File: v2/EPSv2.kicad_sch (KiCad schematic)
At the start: 38 parts, among them J1 Conn_01x02, J2 Conn_01x03, J3 Conn_01x03, J4 5037630491, J5 2P 21700 Cell Holder, J6 5037630491, J7 1053091102, J8 1053091102, J9 1053091102

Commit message: preliminary layout
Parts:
- renumbered J2 to J1, J3 to J2, J1 to J3
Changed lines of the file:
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@@
 		(on_board yes)
 		(dnp no)
-		(property "Reference" "J1"
+		(property "Reference" "J3"
 			(at 65.024 44.958 0)
 			(effects
@@
 			(project ""
 				(path "/61d36b12-c329-4dd2-b08b-b63678fc7b25"
-					(reference "J1")
+					(reference "J3")
 					(unit 1)
 				)
@@
 		(dnp no)
 		(fields_autoplaced yes)
-		(property "Reference" "#PWR08"
+		(property "Reference" "#PWR07"
 			(at 80.01 52.07 0)
 			(effects
@@
 			(project "EPSv2"
 				(path "/61d36b12-c329-4dd2-b08b-b63678fc7b25"
-					(reference "#PWR08")
+					(reference "#PWR07")
 					(unit 1)
 				)
@@
 		(dnp no)
 		(fields_autoplaced yes)
-		(property "Reference" "J2"
+		(property "Reference" "J1"
 			(at 41.91 191.77 0)
 			(effects
@@
 			(project ""
 				(path "/61d36b12-c329-4dd2-b08b-b63678fc7b25"
-					(reference "J2")
+					(reference "J1")
 					(unit 1)
 				)
@@
 		(dnp no)
 		(fields_autoplaced yes)
-		(property "Reference" "J3"
+		(property "Reference" "J2"
 			(at 41.91 212.09 0)
 			(effects
@@
 			(project "EPSv2"
 				(path "/61d36b12-c329-4dd2-b08b-b63678fc7b25"
-					(reference "J3")
+					(reference "J2")
 					(unit 1)
 				)
@@
 		(dnp no)
 		(fields_autoplaced yes)
-		(property "Reference" "#PWR07"
+		(property "Reference" "#PWR08"
 			(at 106.68 55.88 0)
 			(effects
@@
 			(project "EPSv1"
 				(path "/61d36b12-c329-4dd2-b08b-b63678fc7b25"
-					(reference "#PWR07")
+					(reference "#PWR08")
 					(unit 1)
 				)

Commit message: battery charging routing
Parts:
- removed C1, C10, C2, C3, C4, C5, C6, C7, C8, C9: 10uF 0603, Rocketry_Easyeda:C0603, symbol Rocketry_Easyeda:CL10A106KP8NNNC (10uF 0603)
- added C1, C2: 47uF, Capacitor_SMD:C_0603_1608Metric, symbol Device:C
- J4, J6: footprint CON_5037630491 -> Rocketry_Manual:CON_5037630491
- J7, J8, J9: footprint CON_1053091102 -> Rocketry_Manual:CON_1053091102
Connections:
- net +3.3V: now also C1.1
- net GND: now also C1.2, C2.2
- net STM32L432KCUx/+3V3A: now also C2.1
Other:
- moved on the sheet: L1

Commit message: routing done
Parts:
- removed R5, R6, R7: 100k 0603, Rocketry_Easyeda:R0603, symbol Rocketry_Easyeda:0603WAF1003T5E (100k 0603)
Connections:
- net INA199_1/IN- renamed LM7310_9V/VOUT
- net INA199_2/IN- renamed LM7310_5V/VOUT
- net INA199_3/IN- renamed LM7310_3.3V/VOUT
- net PB0 renamed TEMP_1
- net PB1 renamed TEMP_2
- no-connect marks 0 -> 4
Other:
- removed sheet INA199_1
- removed sheet INA199_2
- removed sheet INA199_3
- removed sheet LM66200_4
- removed sheet LM66200_5
- removed sheet LM66200_6
- added sheet LM7310_3.3V (blocks/LM73100.kicad_sch)
- added sheet LM7310_5V (blocks/LM73100.kicad_sch)
- added sheet LM7310_9V (blocks/LM73100.kicad_sch)
- sheet STM32L432KCUx ports: added PB3, PB4, PB5, PB6, PB7; removed none
- note removed: "100k pulldowns to keep the default state ON"
- moved on the sheet: J7, J8, J9

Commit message: CAN txrx
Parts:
- J7, J8, J9: footprint Rocketry_Manual:CON_1053091102 -> Rocketry_Manual:1054301102; symbol Rocketry_Manual:1053091102 -> Rocketry_Manual:1054301102
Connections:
- net GND: now also J4.2 (GND), J6.2 (GND)
- net CAN_TX: now reaches J6.3 (CANH)
- net CAN_TX: now also J4.3 (CANH)
- net CAN_RX: now reaches J6.4 (CANL)
- net CAN_RX: now also J4.4 (CANL)
- no-connect marks 4 -> 2
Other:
- sheet STM32L432KCUx ports: added PA11, PA12; removed PA8
- moved on the sheet: J4

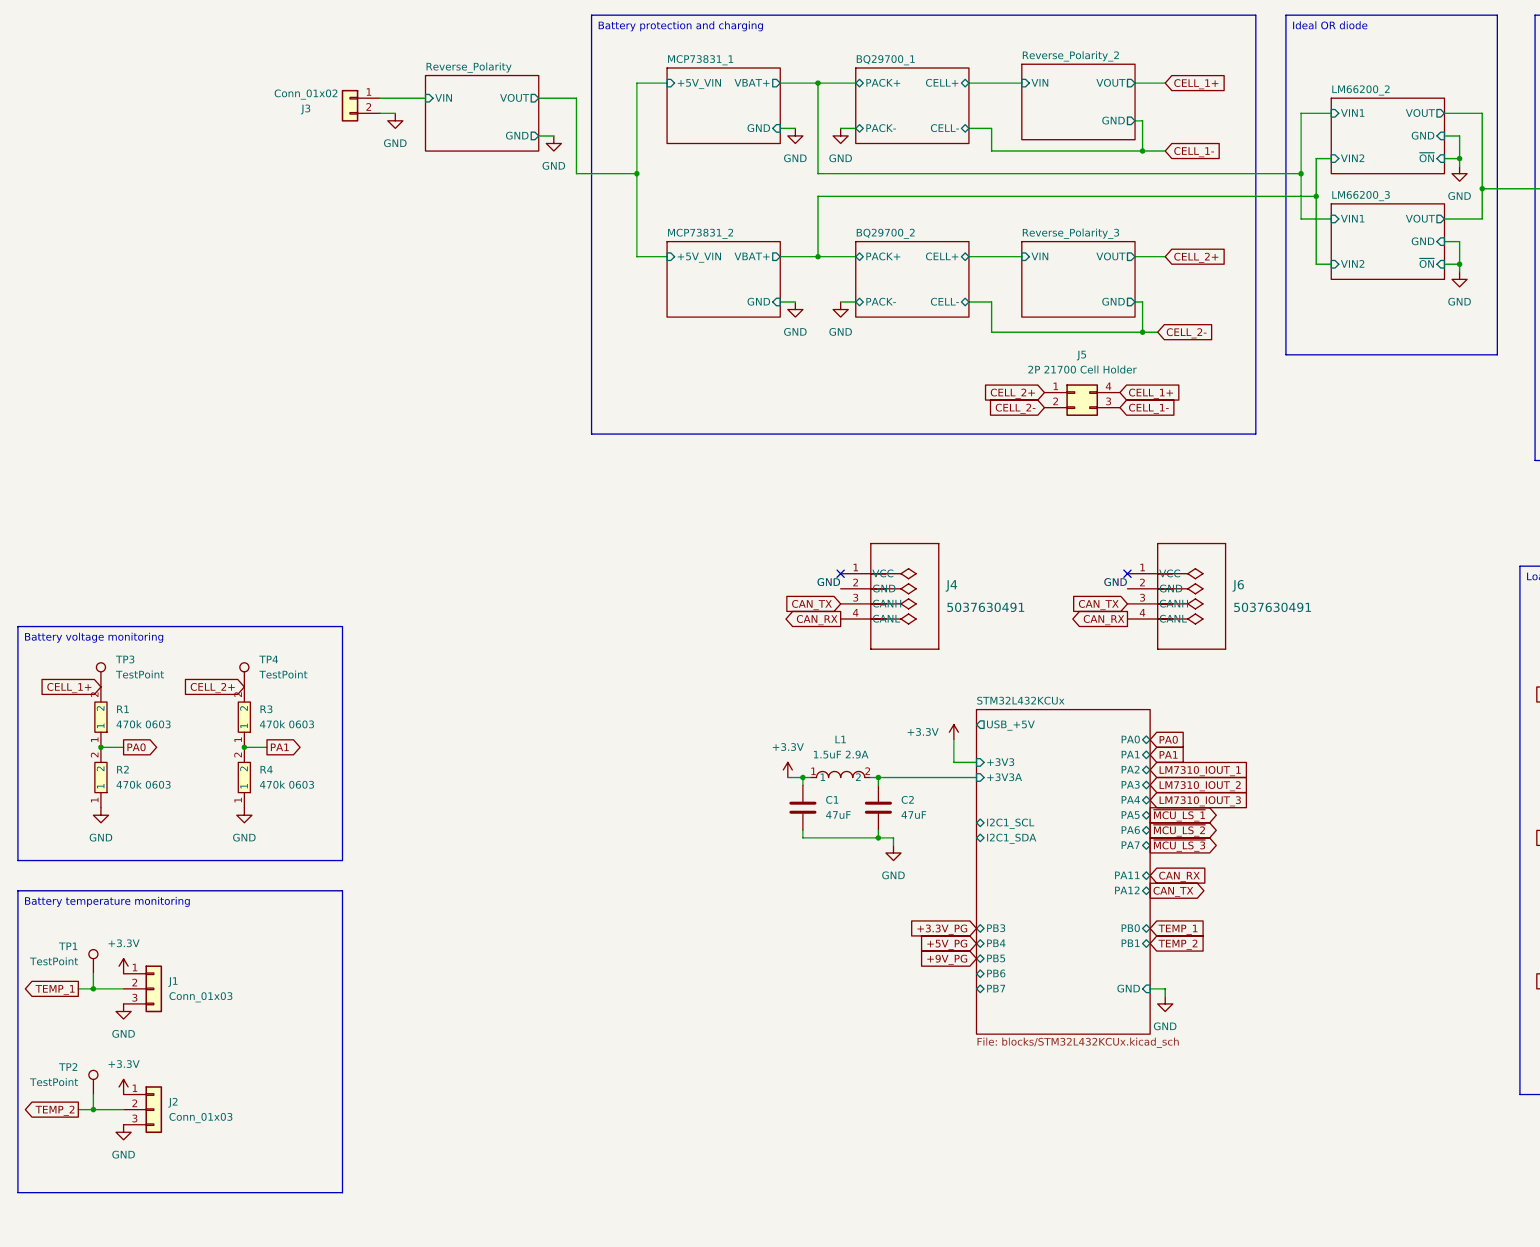
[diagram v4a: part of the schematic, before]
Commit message: can transceiver and battery reverse polarity bypass
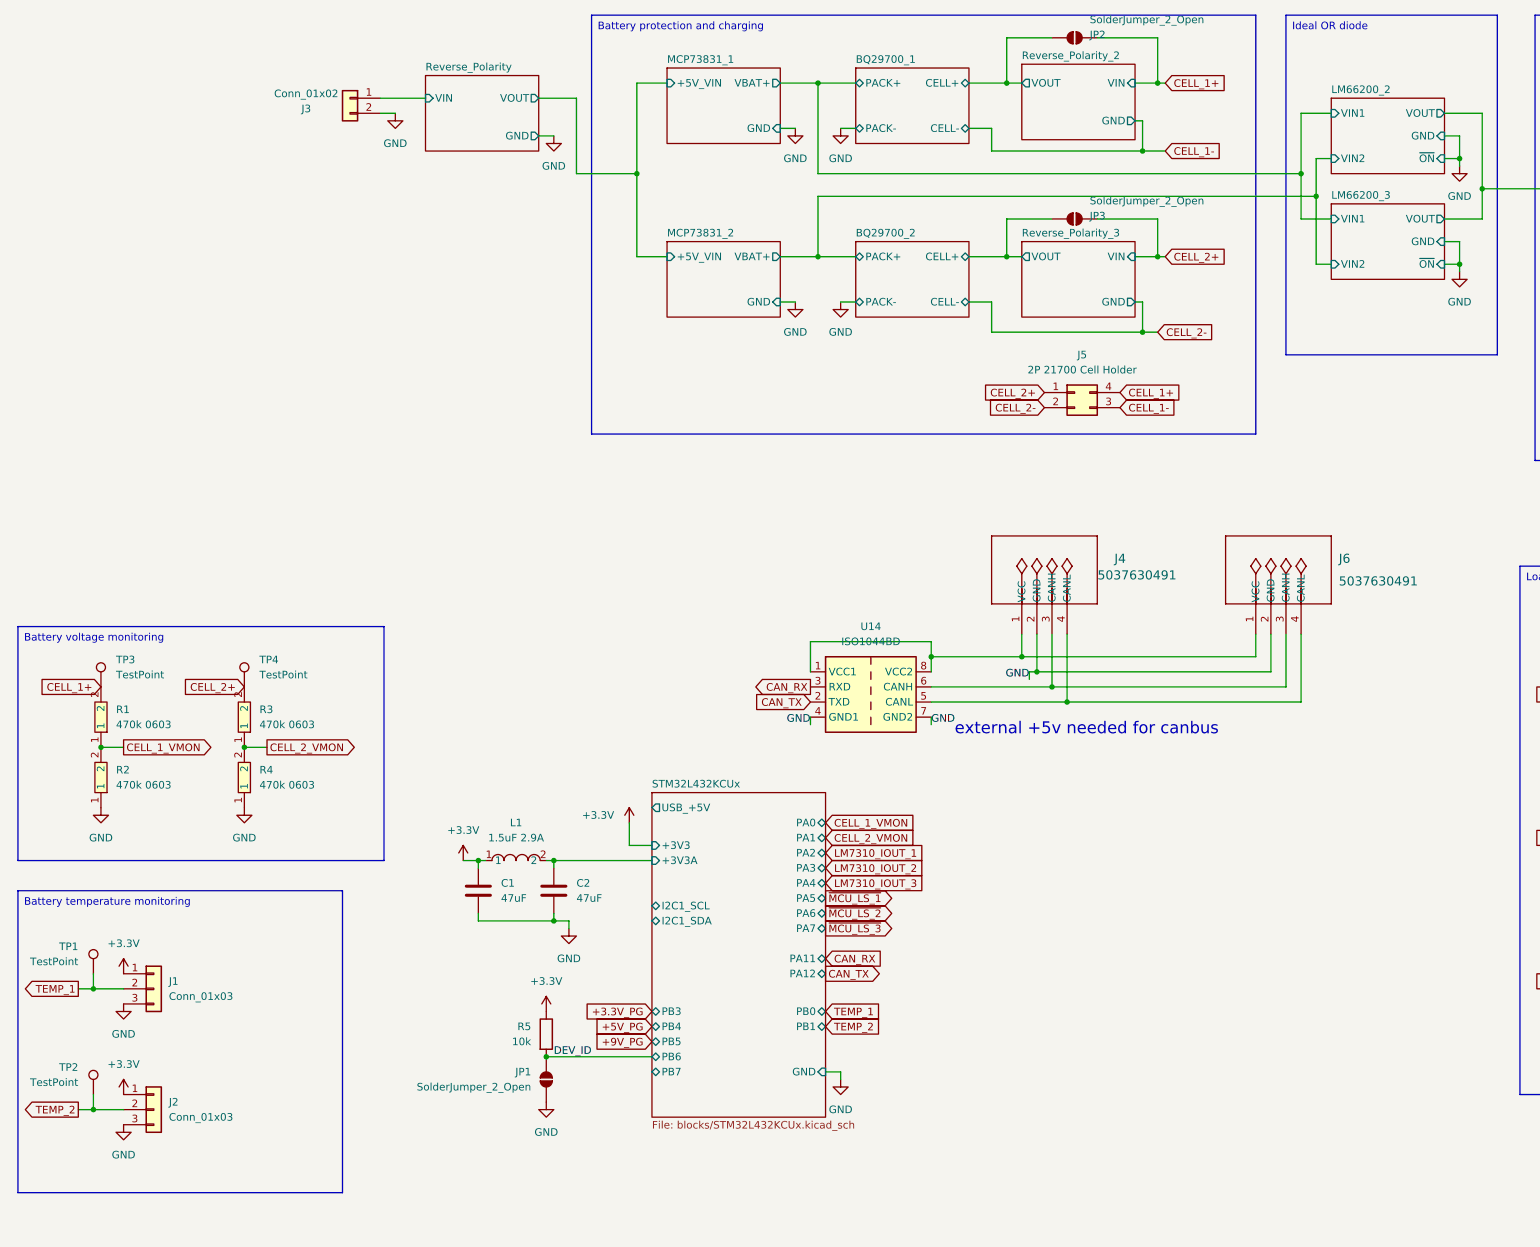
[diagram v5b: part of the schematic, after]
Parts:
- added JP1, JP2, JP3: SolderJumper_2_Open, Jumper:SolderJumper-2_P1.3mm_Open_RoundedPad1.0x1.5mm, symbol Jumper:SolderJumper_2_Open
- added R5: 10k, Resistor_SMD:R_0402_1005Metric, symbol Device:R
- added U14: ISO1044BD, Package_SO:SOIC-8_3.9x4.9mm_P1.27mm, symbol Interface_CAN_LIN:ISO1044BD
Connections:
- net +3.3V: now also R5.1
- net BQ29700_1/CELL+: now also JP2.1 (A)
- net BQ29700_2/CELL+: now also JP3.1 (A)
- net CAN_RX: now also U14.3 (RXD); no longer J4.4 (CANL), J6.4 (CANL)
- net CAN_TX: now also U14.2 (TXD); no longer J4.3 (CANH), J6.3 (CANH)
- net CELL_1+: now also JP2.2 (B)
- net CELL_2+: now also JP3.2 (B)
- net GND: now also JP1.2 (B), U14.4 (GND1), U14.7 (GND2)
- net at J6.1 (VCC): now also J4.1 (VCC), U14.1 (VCC1), U14.8 (VCC2)
- net PA0 renamed CELL_1_VMON
- net PA1 renamed CELL_2_VMON
- new net: J4.3 (CANH), J6.3 (CANH), U14.6 (CANH)
- new net: J4.4 (CANL), J6.4 (CANL), U14.5 (CANL)
- new net DEV_ID: JP1.1 (A), R5.2
- no-connect marks 2 -> 0
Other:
- note added: "external +5v needed for canbus"
- moved on the sheet: C1, C2, J4, J6, L1

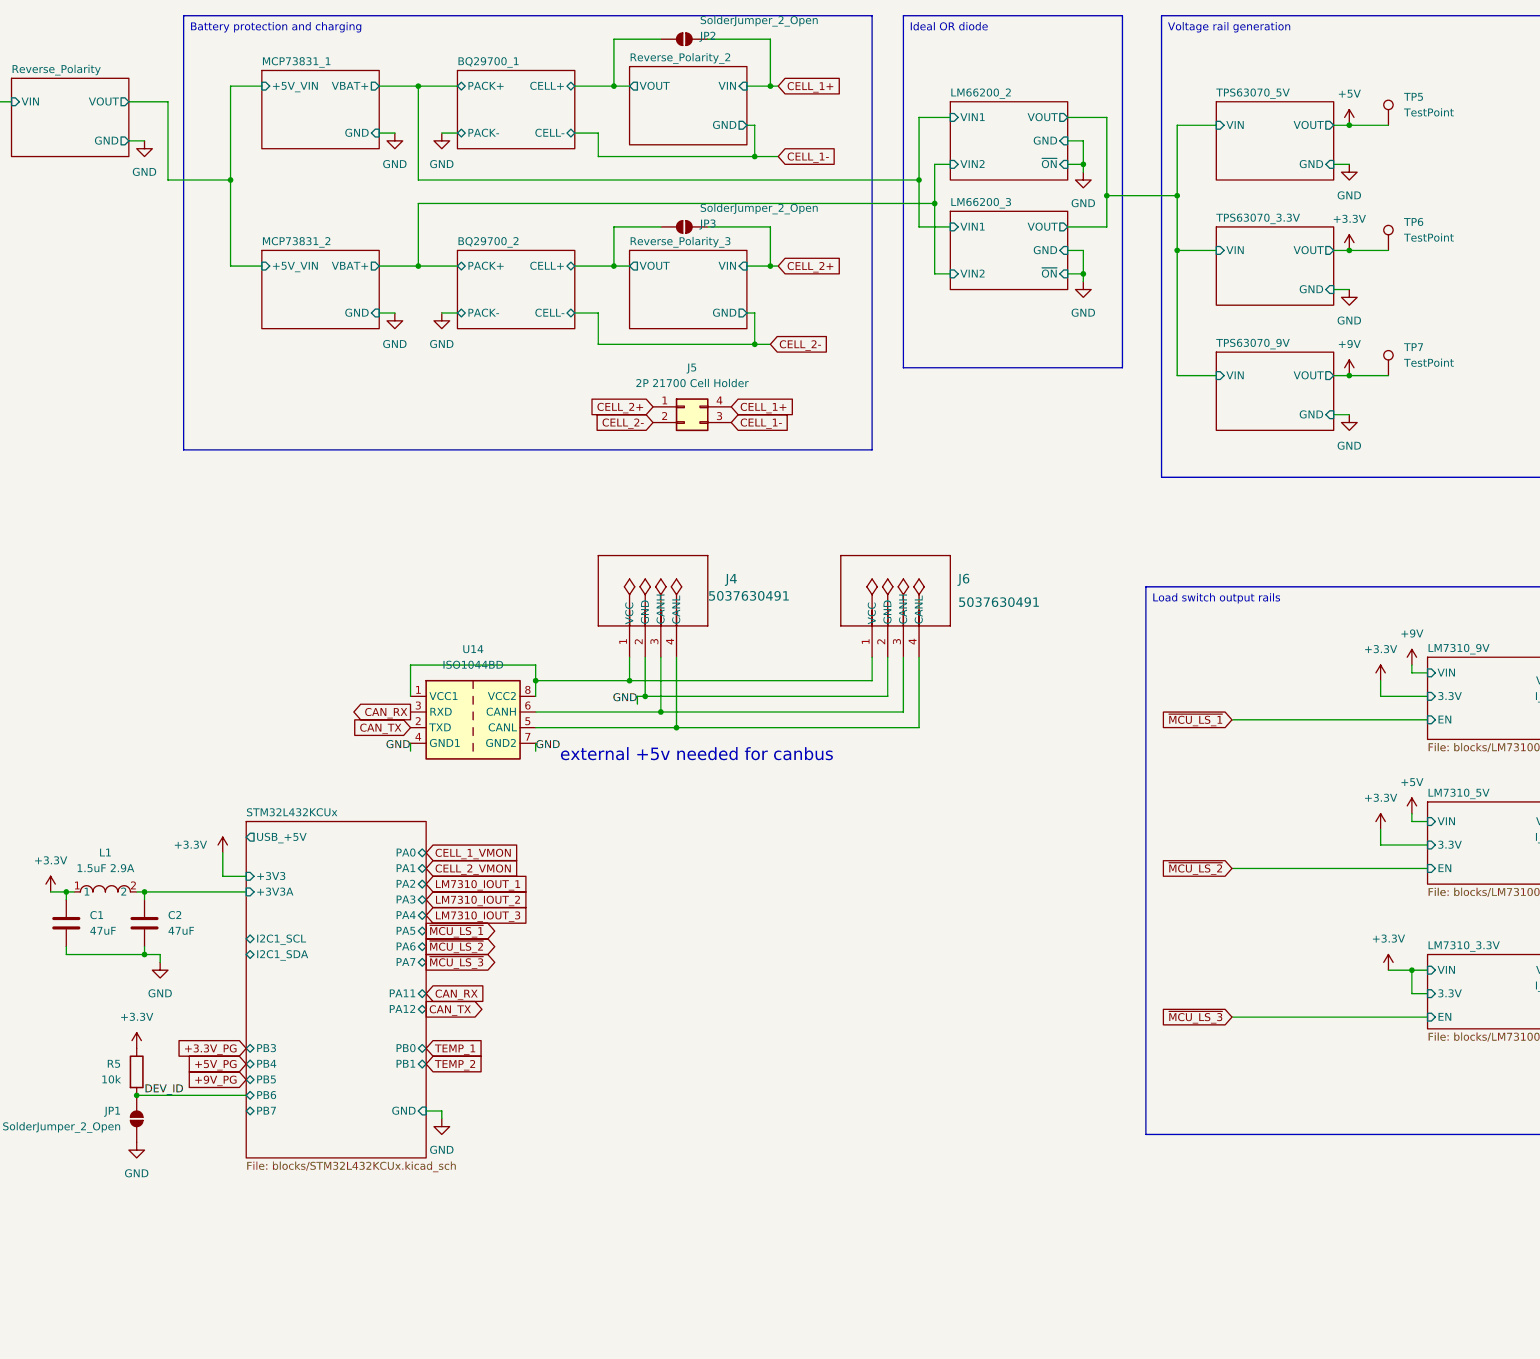
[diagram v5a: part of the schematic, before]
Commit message: bigger current ratings for 5V and 9V
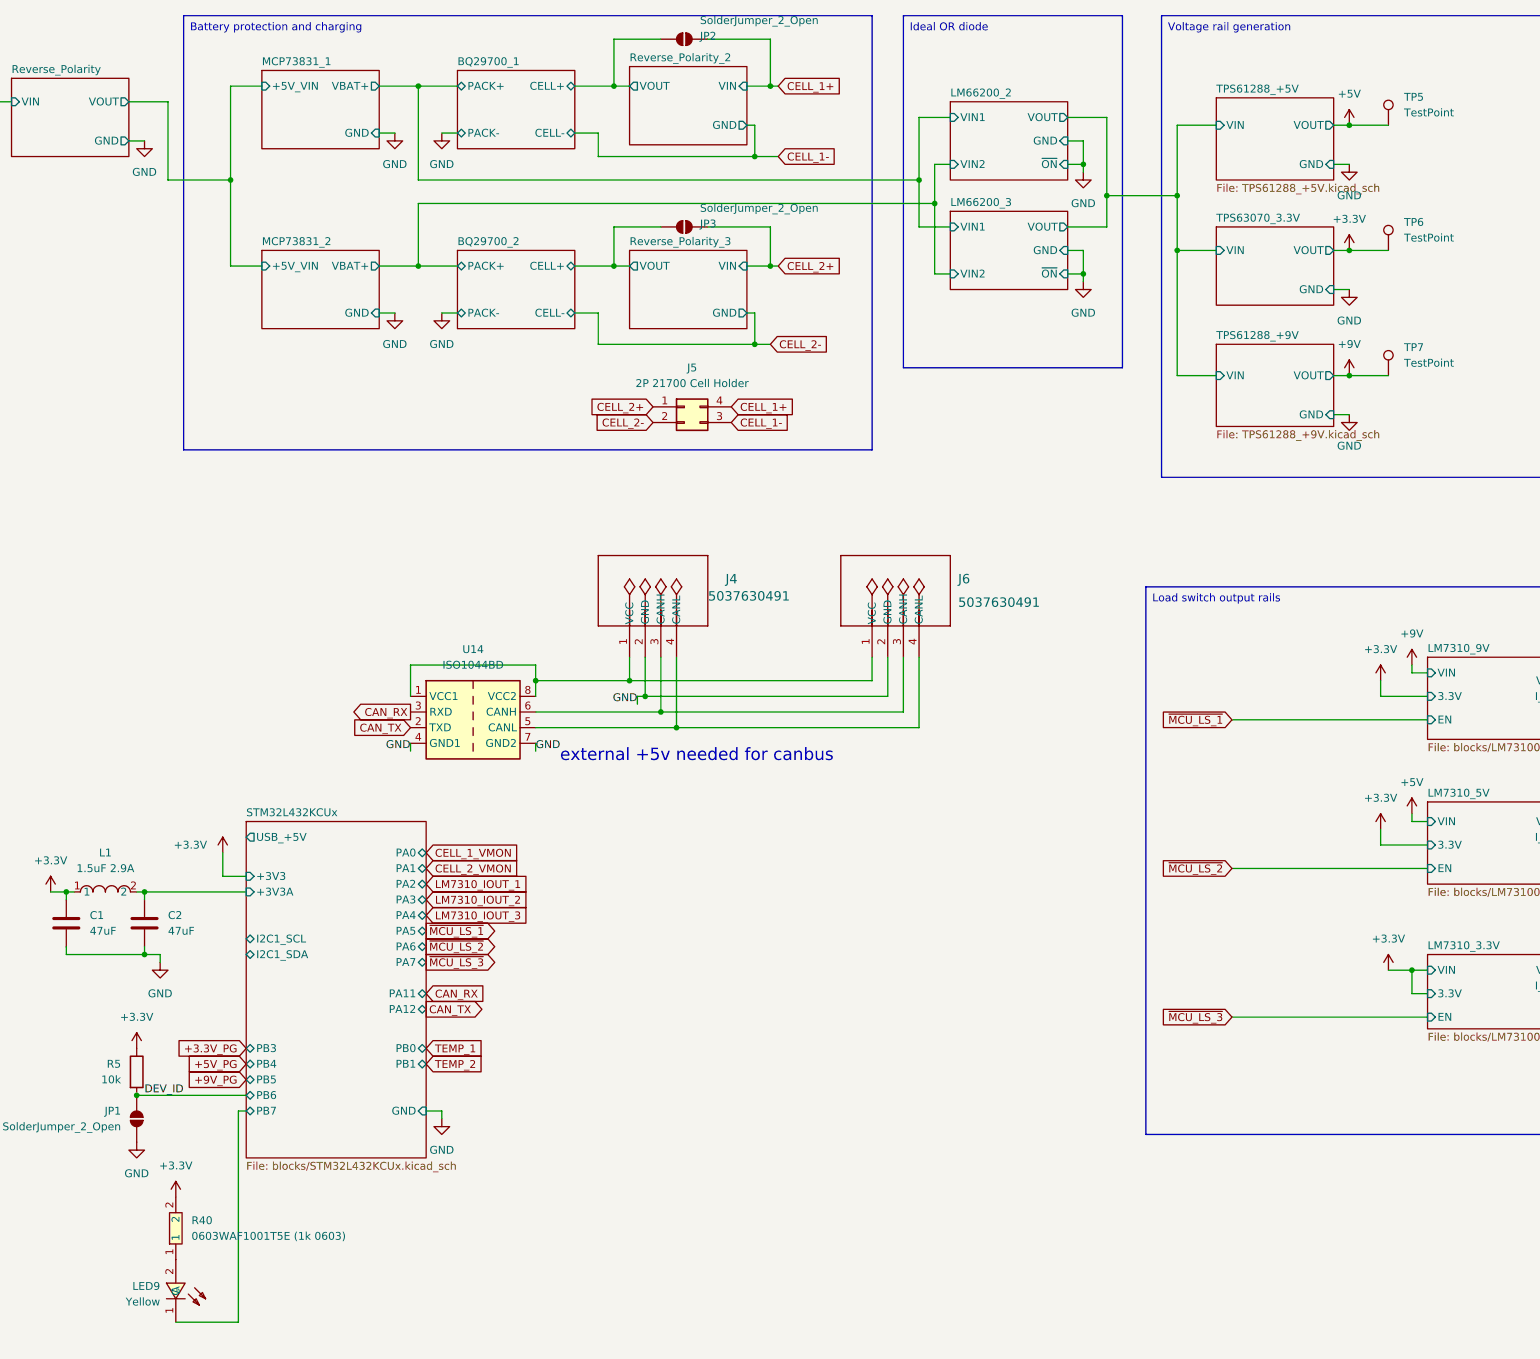
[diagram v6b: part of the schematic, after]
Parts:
- added LED9: Yellow, Rocketry_Easyeda:LED0603-RD-YELLOW, symbol Rocketry_Easyeda:19-213_Y2C-CQ2R2L_3T(CY)
- added R40: 0603WAF1001T5E (1k 0603), Rocketry_Easyeda:R0603, symbol Rocketry_Easyeda:0603WAF1001T5E (1k 0603)
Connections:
- net +3.3V: now also R40.2
- net STM32L432KCUx/PB7: now also LED9.1 (C)
- new net: LED9.2 (A), R40.1
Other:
- removed sheet TPS63070_5V
- removed sheet TPS63070_9V
- added sheet TPS61288_+5V (TPS61288_+5V.kicad_sch)
- added sheet TPS61288_+9V (TPS61288_+9V.kicad_sch)
